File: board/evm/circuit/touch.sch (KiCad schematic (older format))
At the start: 1 part

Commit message: add lots of ICs
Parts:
- removed U?: STM32F405VGTx, LQFP100, symbol STM32F405VGTx
- added U?: MPR121QR2, symbol MPR121QR2
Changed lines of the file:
@@
 EELAYER 25 0
 EELAYER END
-$Descr A2 23386 16535
+$Descr A4 11693 8268
 encoding utf-8
-Sheet 2 8
+Sheet 8 8
 Title ""
 Date ""
@@
 $EndDescr
 $Comp
-L STM32F405VGTx U?
-U 1 1 5753F449
-P 9650 6400
-F 0 "U?" H 5350 9225 50  0000 L BNN
-F 1 "STM32F405VGTx" H 13950 9225 50  0000 R BNN
-F 2 "LQFP100" H 13950 9175 50  0000 R TNN
-F 3 "" H 9650 6400 50  0000 C CNN
-	1    9650 6400
+L MPR121QR2 U?
+U 1 1 57549F10
+P 3850 2950
+F 0 "U?" H 3800 2900 60  0000 C CNN
+F 1 "MPR121QR2" H 3850 3050 60  0000 C CNN
+F 2 "" H 4000 2700 60  0000 C CNN
+F 3 "" H 4000 2700 60  0000 C CNN
+	1    3850 2950
 	1    0    0    -1
 $EndComp

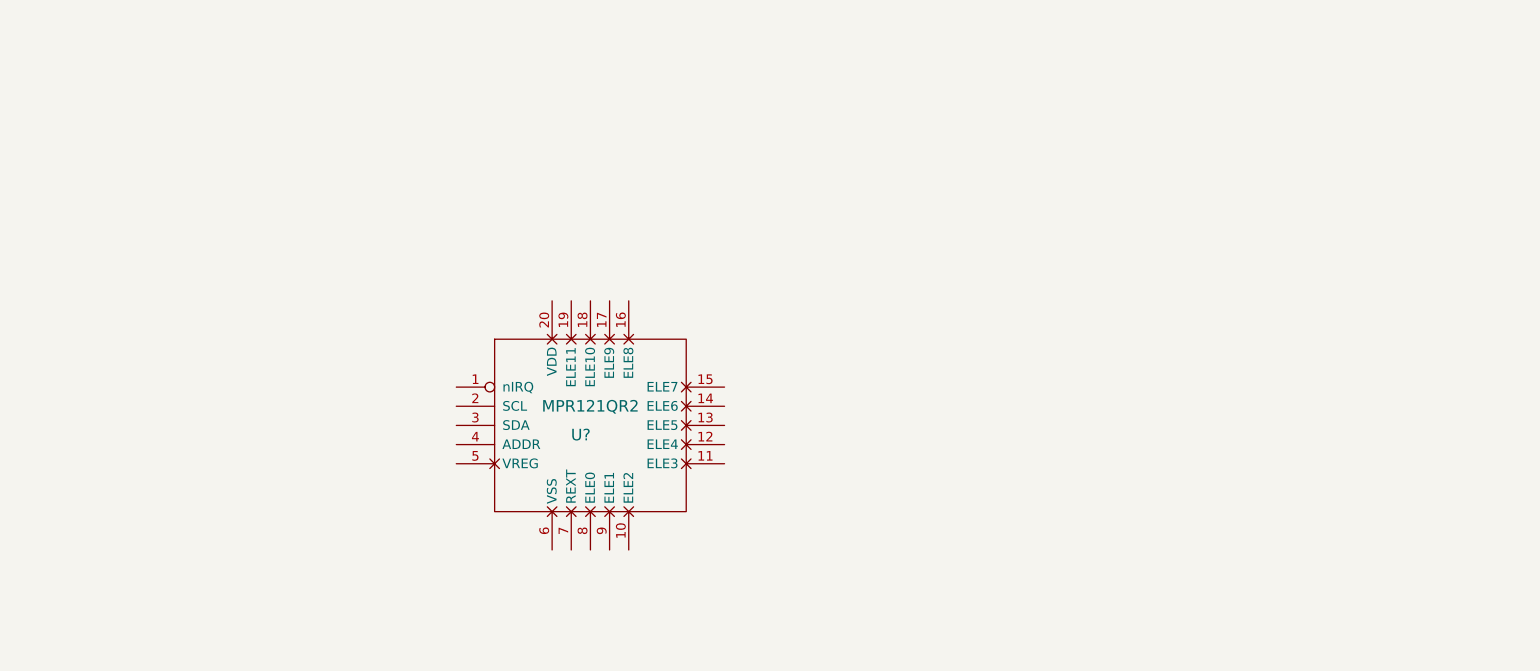
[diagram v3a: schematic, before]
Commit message: still working for sch
All done except for battery, which need more consideration on scheme of
QC2.0 (or QC3.0?), bidirectional charge.
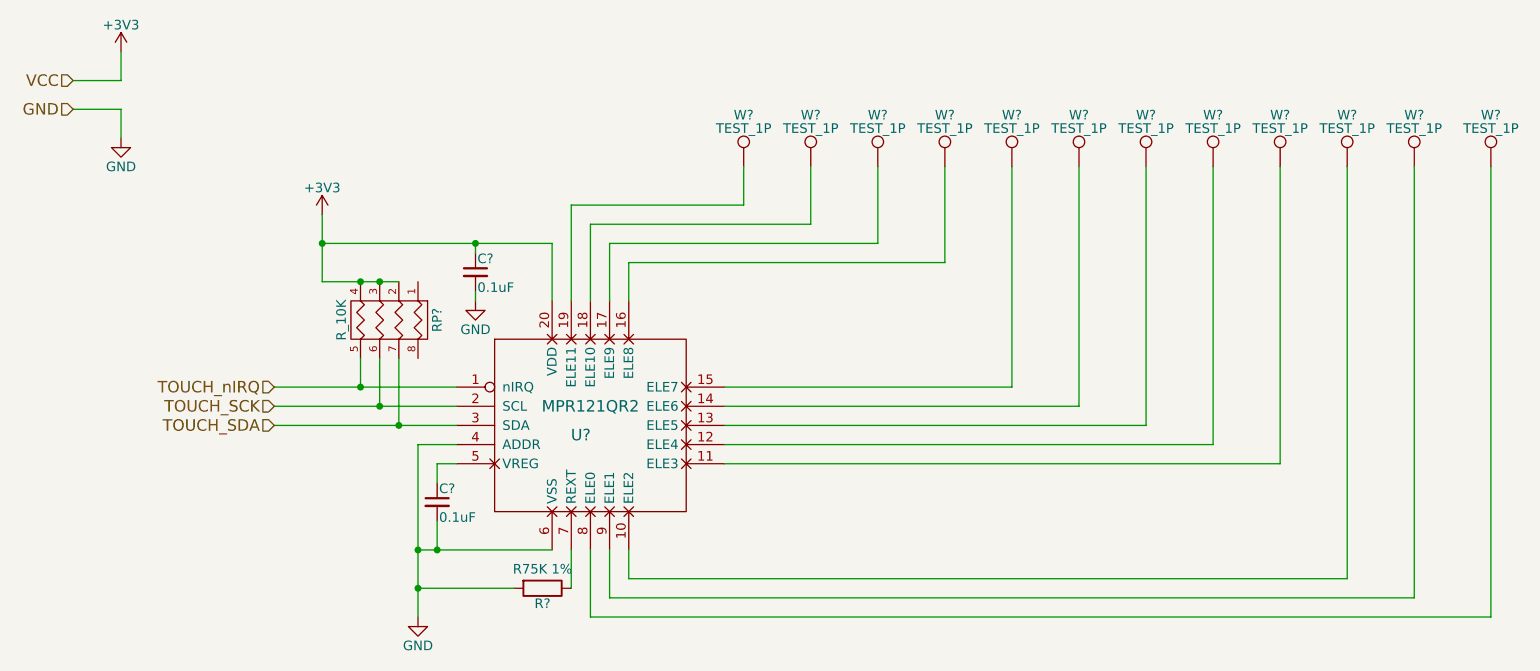
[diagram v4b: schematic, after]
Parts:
- added C? (x2): 0.1uF, symbol C_Small
- added R?: R75K 1%, symbol R
- added RP?: R_10K, symbol R_PACK4
- added W? (x12): TEST_1P, symbol TEST_1P
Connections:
- net TOUCH_nIRQ: now reaches U?.1 (nIRQ)
- net TOUCH_nIRQ: now also RP?.5 (R4)
- net at U?.10 (ELE2): now also W?.1
- net at U?.11 (ELE3): now also W?.1
- net at U?.12 (ELE4): now also W?.1
- net at U?.13 (ELE5): now also W?.1
- net at U?.14 (ELE6): now also W?.1
- net at U?.15 (ELE7): now also W?.1
- net at U?.16 (ELE8): now also W?.1
- net at U?.17 (ELE9): now also W?.1
- net at U?.18 (ELE10): now also W?.1
- net at U?.19 (ELE11): now also W?.1
- net TOUCH_SCK: now reaches U?.2 (SCL)
- net TOUCH_SCK: now also RP?.6 (R3)
- net +3V3: now reaches U?.20 (VDD)
- net +3V3: now also C?.1, RP?.2 (P2), RP?.3 (P3), RP?.4 (P4)
- net TOUCH_SDA: now reaches U?.3 (SDA)
- net TOUCH_SDA: now also RP?.7 (R2)
- net GND: now reaches U?.4 (ADDR)
- net GND: now also U?.6 (VSS), C?.2, C?.2, R?.2
- net at U?.5 (VREG): now also C?.1
- net at U?.7 (REXT): now also R?.1
- net at U?.8 (ELE0): now also W?.1
- net at U?.9 (ELE1): now also W?.1
